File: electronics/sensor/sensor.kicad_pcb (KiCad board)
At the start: 2 copper layers, 16.3 x 16.3 mm, 3 parts, among them P100 SENSOR, U100 AH3391Q

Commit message: Update older KiCad projects to KiCad 5 (#150)
- Updates Classic Controller and Sensor PCB project files for KiCad 5 (minimal functionality migration; symbols and footprints are mostly unchanged)
- Updates CI to panelize and export gerbers using kikit
- Removes legacy electronics CI action; all electronics artifacts are generated in a single github action
- Removes old panelize and BOM-export scripts

Fixes #138
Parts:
- H1: renamed from Z1; value MOUNT -> MountingHole_Pad
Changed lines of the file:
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@@
-(kicad_pcb (version 4) (host pcbnew 4.0.7)
+(kicad_pcb (version 20171130) (host pcbnew 5.1.9-73d0e3b20d~88~ubuntu20.04.1)
   (general
-    (links 3)
-    (no_connects 0)
-    (area 19.924999 19.924999 36.331001 36.331001)
     (thickness 1.6)
     (drawings 18)
@@
     (zone_45_only yes)
     (trace_min 0.2)
-    (segment_width 0.2)
-    (edge_width 0.15)
     (via_size 0.6)
     (via_drill 0.4)
@@
     (uvia_min_size 0.2)
     (uvia_min_drill 0.1)
+    (edge_width 0.15)
+    (segment_width 0.2)
     (pcb_text_width 0.3)
     (pcb_text_size 1.5 1.5)
@@
       (layerselection 0x010f0_80000001)
       (usegerberextensions false)
+      (usegerberattributes true)
+      (usegerberadvancedattributes true)
+      (creategerberjobfile true)
       (excludeedgelayer false)
       (linewidth 0.100000)
@@
       (hpglpennumber 1)
       (hpglpenspeed 20)
-      (hpglpendiameter 15)
-      (hpglpenoverlay 2)
+      (hpglpendiameter 15.000000)
       (psnegative false)
       (psa4output false)
@@
       (drillshape 1)
       (scaleselection 1)
-      (outputdirectory build/))
+      (outputdirectory "build/"))
   )
   (net 0 "")
@@
     (uvia_dia 0.3)
     (uvia_drill 0.1)
+    (add_net "Net-(H1-Pad1)")
     (add_net "Net-(P100-Pad1)")
     (add_net "Net-(P100-Pad2)")
@@
     (uvia_drill 0.1)
   )
+  (module MountingHoles:M4_mount (layer F.Cu)
+    (at 24.572 24.572)
+    (fp_text reference H1 (at 0 1.7) (layer F.SilkS) hide
+      (effects (font (size 1 1) (thickness 0.15)))
+    )
+    (fp_text value MountingHole_Pad (at 0 -1.5) (layer F.Fab) hide
+      (effects (font (size 1 1) (thickness 0.15)))
+    )
+    (fp_circle (center 0 0) (end 4 0) (layer F.SilkS) (width 0.15))
+    (pad 1 thru_hole circle (at 0 0) (size 5.5 5.5) (drill 4.5) (layers *.Cu *.Mask F.SilkS)
+      (clearance 1.5))
+  )
   (module PinHeaders:Pin_Header_Straight_1x03 (layer F.Cu)
     (at 33.208 33.208 270)
     (descr "Through hole pin header")
     (tags "pin header")
-    (fp_text reference P100 (at -2.032 0 360) (layer F.SilkS) hide
+    (fp_text reference P100 (at -2.032 0) (layer F.SilkS) hide
       (effects (font (size 1 1) (thickness 0.15)))
     )
-    (fp_text value SENSOR (at -2.032 4.318 360) (layer F.Fab) hide
+    (fp_text value SENSOR (at -2.032 4.318) (layer F.Fab) hide
       (effects (font (size 1 1) (thickness 0.15)))
     )
@@
       (net 3 "Net-(P100-Pad3)"))
     (model Pin_Headers.3dshapes/Pin_Header_Straight_1x03.wrl
-      (at (xyz 0 -0.1 0))
+      (offset (xyz 0 -2.539999961853027 0))
       (scale (xyz 1 1 1))
       (rotate (xyz 0 0 90))
     )
   )
-  (module MountingHoles:M4_mount (layer F.Cu)
-    (at 24.572 24.572)
-    (fp_text reference Z1 (at 0 1.7) (layer F.SilkS) hide
-      (effects (font (size 1 1) (thickness 0.15)))
-    )
-    (fp_text value MOUNT (at 0 -1.5) (layer F.Fab) hide
-      (effects (font (size 1 1) (thickness 0.15)))
-    )
-    (fp_circle (center 0 0) (end 4 0) (layer F.SilkS) (width 0.15))
-    (pad 1 thru_hole circle (at 0 0) (size 5.5 5.5) (drill 4.5) (layers *.Cu *.Mask F.SilkS)
-      (clearance 1.5))
-  )
   (module hall_effect:hall_effect (layer B.Cu)

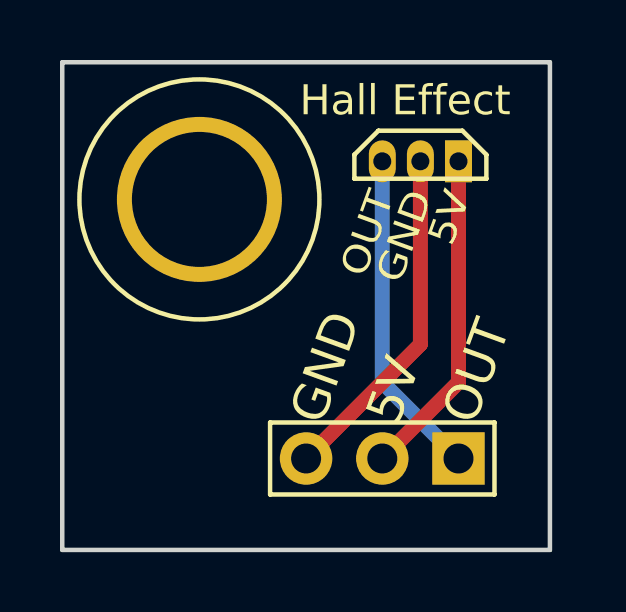
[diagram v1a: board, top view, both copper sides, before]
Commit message: Sensor PCB improvements
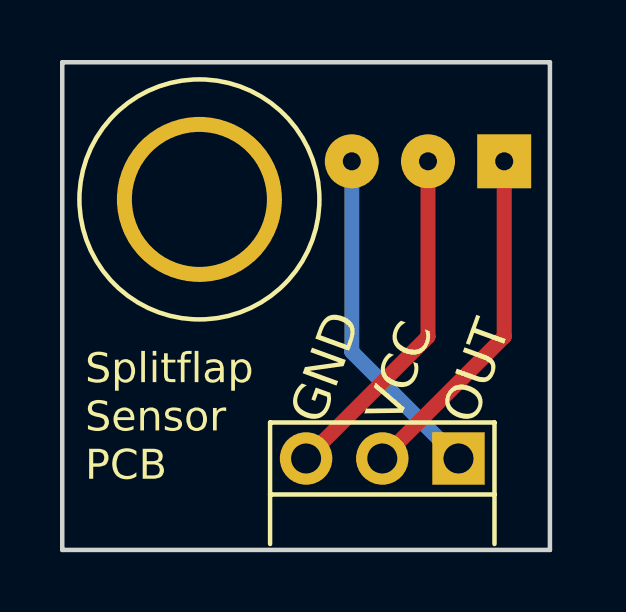
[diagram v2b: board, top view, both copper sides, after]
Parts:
- U100: footprint hall_effect:hall_effect -> hall_effect:hall_effect_wide
- moved U100 0.25 mm to (32.2, 23.3)
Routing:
- net Net-(P100-Pad2): track 11.0 -> 11.6 mm
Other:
- board text added: "Splitflap Sensor PCB"
- board text added: "VCC"
- board text removed: "5V"

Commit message: Label sensor PCB v1.1 and add 3d models
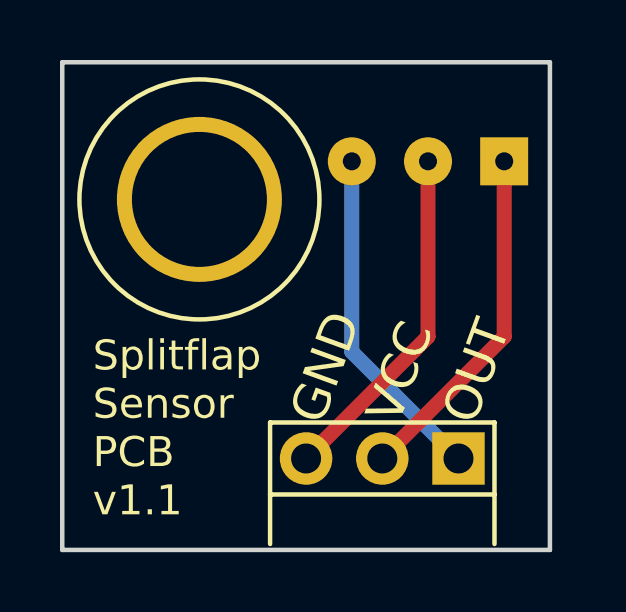
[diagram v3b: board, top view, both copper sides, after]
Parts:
- P100: footprint PinHeaders:Pin_Header_Straight_1x03 -> ModifiedSymbols:Pin_Header_Right_Angle_1x03
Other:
- board text added: "Splitflap Sensor PCB v1.1"
- board text removed: "Splitflap Sensor PCB"
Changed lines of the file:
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@@
     (uvia_dia 0.3)
     (uvia_drill 0.1)
+    (add_net "Net-(H1-Pad1)")
     (add_net "Net-(P100-Pad1)")
     (add_net "Net-(P100-Pad2)")
@@
     (uvia_drill 0.1)
   )
+  (module ModifiedSymbols:Pin_Header_Right_Angle_1x03 (layer F.Cu)
+    (at 33.208 33.208 270)
+    (descr "Through hole pin header")
+    (tags "pin header")
+    (fp_text reference P100 (at -2.032 0) (layer F.SilkS) hide
+      (effects (font (size 1 1) (thickness 0.15)))
+    )
+    (fp_text value SENSOR (at -2.032 4.318) (layer F.Fab) hide
+      (effects (font (size 1 1) (thickness 0.15)))
+    )
+    (fp_line (start -1.2 6.28) (end 1.2 6.28) (layer F.SilkS) (width 0.15))
+    (fp_line (start -1.2 -1.2) (end -1.2 6.28) (layer F.SilkS) (width 0.15))
+    (fp_line (start 1.2 -1.2) (end 1.2 6.28) (layer F.SilkS) (width 0.15))
+    (fp_line (start -1.2 -1.2) (end 1.2 -1.2) (layer F.SilkS) (width 0.15))
+    (pad 3 thru_hole circle (at 0 5.08 270) (size 1.75 1.75) (drill 1) (layers *.Cu *.Mask)
+      (net 3 "Net-(P100-Pad3)"))
+    (pad 2 thru_hole circle (at 0 2.54 270) (size 1.75 1.75) (drill 1) (layers *.Cu *.Mask)
+      (net 2 "Net-(P100-Pad2)"))
+    (pad 1 thru_hole rect (at 0 0 270) (size 1.75 1.75) (drill 1) (layers *.Cu *.Mask)
+      (net 1 "Net-(P100-Pad1)"))
+    (model ${KISYS3DMOD}/Connector_PinHeader_2.54mm.3dshapes/PinHeader_1x03_P2.54mm_Horizontal.step
+      (at (xyz 0 0 0))
+      (scale (xyz 1 1 1))
+      (rotate (xyz 0 0 0))
+    )
+  )
   (module hall_effect:hall_effect_wide (layer B.Cu)
     (at 32.192 23.302 180)
@@
       (effects (font (size 1 1) (thickness 0.15)) (justify mirror))
     )
+    (fp_line (start -2.2 0.889) (end 2.2 0.889) (layer B.SilkS) (width 0.15))
+    (fp_line (start -2.2 0.889) (end -2.2 3.175) (layer B.SilkS) (width 0.15))
+    (fp_line (start 2.2 0.889) (end 2.2 3.175) (layer B.SilkS) (width 0.15))
+    (fp_line (start -1.397 3.175) (end -1.397 0.889) (layer B.SilkS) (width 0.15))
     (fp_line (start 1.397 3.175) (end 1.4 0.889) (layer B.SilkS) (width 0.15))
-    (fp_line (start -1.397 3.175) (end -1.397 0.889) (layer B.SilkS) (width 0.15))
-    (fp_line (start 2.2 0.889) (end 2.2 3.175) (layer B.SilkS) (width 0.15))
-    (fp_line (start -2.2 0.889) (end -2.2 3.175) (layer B.SilkS) (width 0.15))
-    (fp_line (start -2.2 0.889) (end 2.2 0.889) (layer B.SilkS) (width 0.15))
-    (pad 3 thru_hole circle (at 2.54 0 180) (size 1.8 1.8) (drill 0.6) (layers *.Cu *.Mask)
+    (pad 3 thru_hole circle (at 2.54 0 180) (size 1.6 1.6) (drill 0.6) (layers *.Cu *.Mask)
       (net 1 "Net-(P100-Pad1)"))
-    (pad 2 thru_hole circle (at 0 0 180) (size 1.8 1.8) (drill 0.6) (layers *.Cu *.Mask)
+    (pad 2 thru_hole circle (at 0 0 180) (size 1.6 1.6) (drill 0.6) (layers *.Cu *.Mask)
       (net 3 "Net-(P100-Pad3)"))
-    (pad 1 thru_hole rect (at -2.54 0 180) (size 1.8 1.8) (drill 0.6) (layers *.Cu *.Mask)
+    (pad 1 thru_hole rect (at -2.54 0 180) (size 1.6 1.6) (drill 0.6) (layers *.Cu *.Mask)
       (net 2 "Net-(P100-Pad2)"))
+    (model ${KISYS3DMOD}/Package_TO_SOT_THT.3dshapes/TO-92S_Wide.step
+      (offset (xyz 2.54 0 2.5))
+      (scale (xyz 1 1 1))
+      (rotate (xyz 0 0 180))
+    )
   )
   (module MountingHoles:M4_mount (layer F.Cu)
@@
     (pad 1 thru_hole circle (at 0 0) (size 5.5 5.5) (drill 4.5) (layers *.Cu *.Mask F.SilkS)
       (clearance 1.5))
-  )
-  (module PinHeaders:Pin_Header_Straight_1x03 (layer F.Cu)
-    (at 33.208 33.208 270)
-    (descr "Through hole pin header")
-    (tags "pin header")
-    (fp_text reference P100 (at -2.032 0) (layer F.SilkS) hide
-      (effects (font (size 1 1) (thickness 0.15)))
-    )
-    (fp_text value SENSOR (at -2.032 4.318) (layer F.Fab) hide
-      (effects (font (size 1 1) (thickness 0.15)))
-    )
-    (fp_line (start -1.2 -1.2) (end 1.2 -1.2) (layer F.SilkS) (width 0.15))
-    (fp_line (start 1.2 -1.2) (end 1.2 6.28) (layer F.SilkS) (width 0.15))
-    (fp_line (start -1.2 -1.2) (end -1.2 6.28) (layer F.SilkS) (width 0.15))
-    (fp_line (start -1.2 6.28) (end 1.2 6.28) (layer F.SilkS) (width 0.15))
-    (pad 1 thru_hole rect (at 0 0 270) (size 1.75 1.75) (drill 1) (layers *.Cu *.Mask F.SilkS)
-      (net 1 "Net-(P100-Pad1)"))
-    (pad 2 thru_hole circle (at 0 2.54 270) (size 1.75 1.75) (drill 1) (layers *.Cu *.Mask F.SilkS)
-      (net 2 "Net-(P100-Pad2)"))
-    (pad 3 thru_hole circle (at 0 5.08 270) (size 1.75 1.75) (drill 1) (layers *.Cu *.Mask F.SilkS)
-      (net 3 "Net-(P100-Pad3)"))
-    (model Pin_Headers.3dshapes/Pin_Header_Straight_1x03.wrl
-      (offset (xyz 0 -2.539999961853027 0))
-      (scale (xyz 1 1 1))
-      (rotate (xyz 0 0 90))
-    )
   )
   (gr_line (start 34.408 34.408) (end 34.408 36.059) (layer F.SilkS) (width 0.15))
@@
   )
   (gr_line (start 20 20) (end 36.256 20) (angle 90) (layer Edge.Cuts) (width 0.15))
-  (gr_text "Splitflap\nSensor\nPCB" (at 20.762 31.811) (layer F.SilkS)
+  (gr_text "Splitflap\nSensor\nPCB\nv1.1" (at 21.016 32.192) (layer F.SilkS)
     (effects (font (size 1 1) (thickness 0.15)) (justify left))
   )
